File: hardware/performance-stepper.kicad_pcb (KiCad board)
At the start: 4 copper layers, 80 x 80 mm, 114 parts, among them P1 VIN, P101 CON-SENSOR2, P102 DEBUG, P103 BOOT, P2 OUT, P3 GPIO, P4 PROTO, P5 L, P6 M, P7 S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

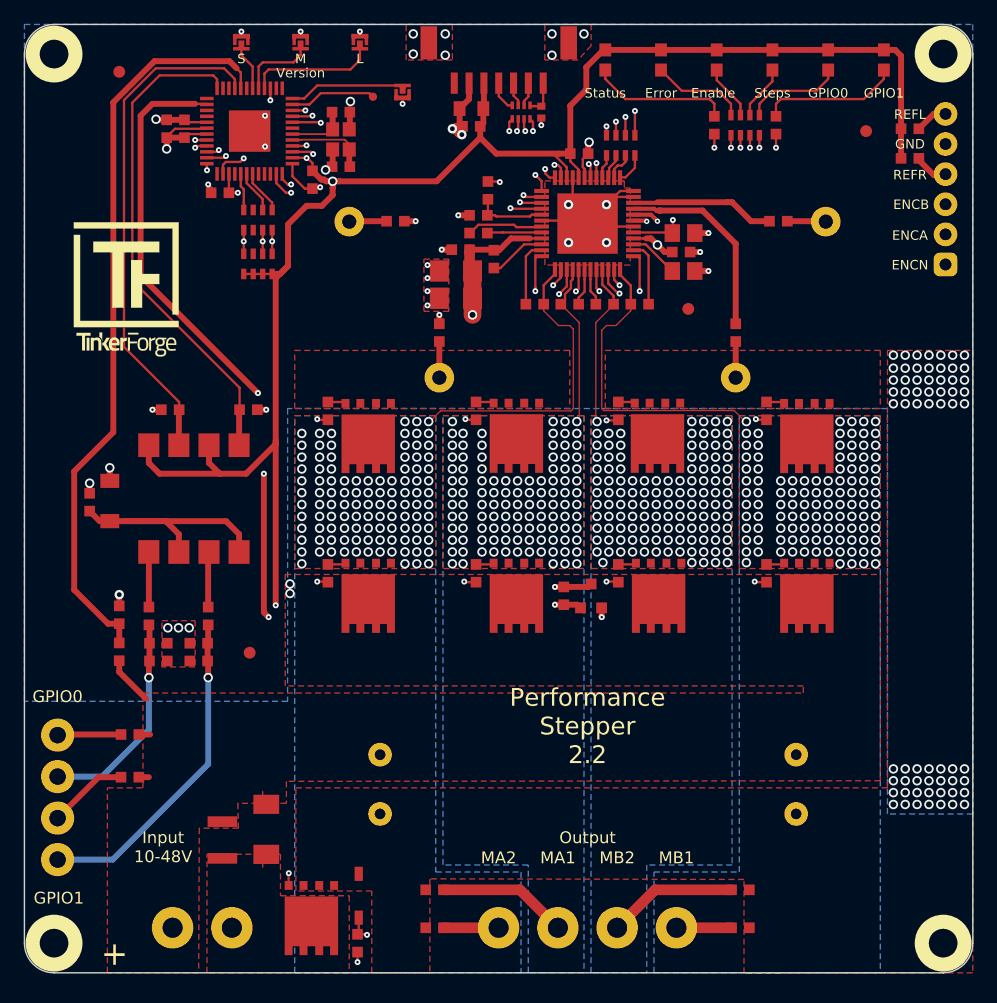
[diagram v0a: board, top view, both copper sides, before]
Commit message: changed version number, changed silkscreen
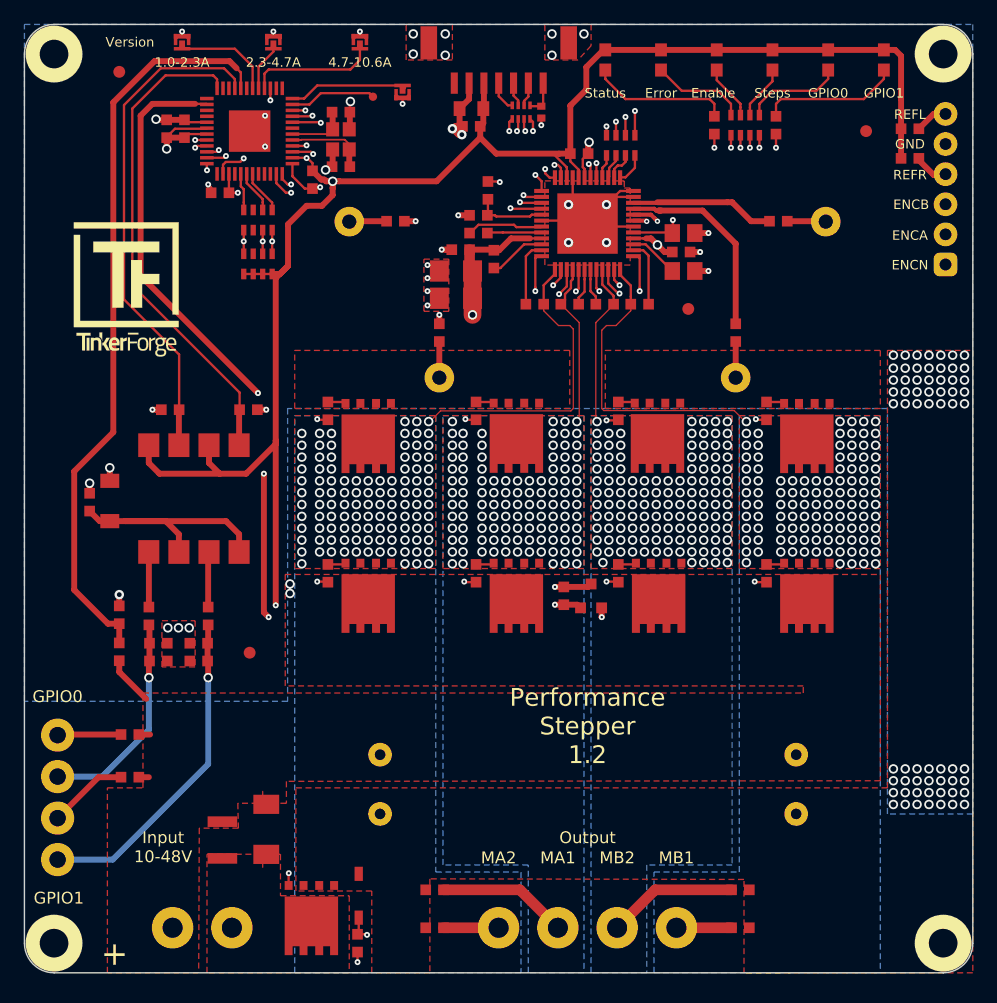
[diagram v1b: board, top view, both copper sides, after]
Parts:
- R10, R11: value . -> DNP
- moved P7 5.00 mm to (58.3, 91.5)
- moved P6 2.30 mm to (66.0, 91.5)
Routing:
- net Net-(P7-Pad2): track 4.13 -> 8.81 mm
- net Net-(P6-Pad2): track 6.73 -> 4.26 mm
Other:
- board text added: "1.0-2.3A"
- board text added: "2.3-4.7A"
- board text added: "4.7-10.6A"
- board text added: "Performance Stepper 1.2"
- board text removed: "L"
- board text removed: "M"
- board text removed: "Performance Stepper 2.2"
- board text removed: "S"
